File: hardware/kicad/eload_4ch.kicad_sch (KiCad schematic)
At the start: 0 parts

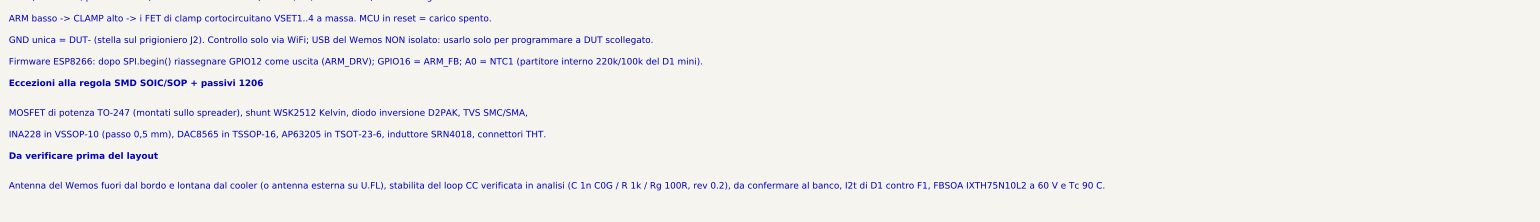
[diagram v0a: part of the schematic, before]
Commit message: rev 0.3: front panel with I2C OLED, encoder and OUTPUT button
PCF8574 expander (0x20) with INT on GPIO0, 10-pin IDC connector,
RC debounce, I2C pull-ups 2.2k, re-routed PCB (DRC/parity clean),
updated BOM, slides (front panel page) and README.

Co-Authored-By: Claude Opus 5.5 <noreply@anthropic.com>
Claude-Session: https://claude.ai/code/session_013KrwoEq2Y4F9LNKutY5RJ4
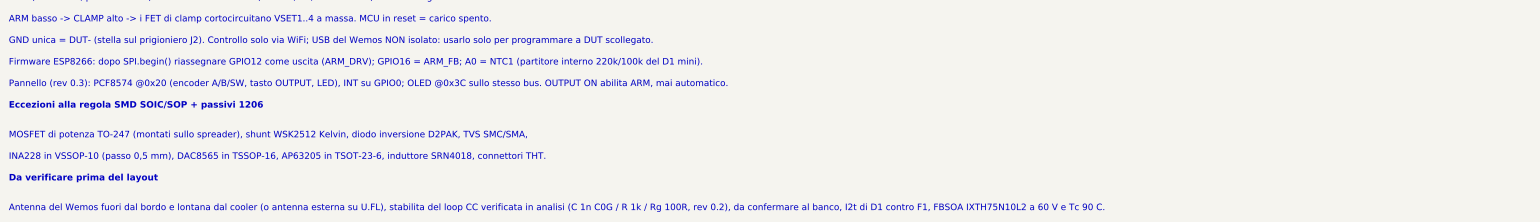
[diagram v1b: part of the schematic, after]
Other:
- note added: "Pannello (rev 0.3): PCF8574 @0x20 (encoder A/B/SW, tasto OUTPUT, LED), INT su GPIO0; OLED @0x3C sullo stesso bus. OUTPUT ON abilita ARM, mai automatico."
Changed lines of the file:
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@@
 		(title "Carico attivo 60V 20A 300W — Indice")
 		(date "2026-10-25")
-		(rev "0.2")
+		(rev "0.3")
 		(company "IV3HGA")
 		(comment 1 "Schema gerarchico: un foglio per blocco funzionale")
 	)
+	(text "GND unica = DUT- (stella sul prigioniero J2). Controllo solo via WiFi; USB del Wemos NON isolato: usarlo solo per programmare a DUT scollegato."
+		(exclude_from_sim no)
+		(at 30 212.32 0)
+		(effects
+			(font
+				(size 1.524 1.524)
+			)
+			(justify left bottom)
+		)
+	)
+	(text "Da verificare prima del layout"
+		(exclude_from_sim no)
+		(at 30 244.72 0)
+		(effects
+			(font
+				(size 1.524 1.524)
+				(bold yes)
+			)
+			(justify left bottom)
+		)
+	)
+	(text "Pannello (rev 0.3): PCF8574 @0x20 (encoder A/B/SW, tasto OUTPUT, LED), INT su GPIO0; OLED @0x3C sullo stesso bus. OUTPUT ON abilita ARM, mai automatico."
+		(exclude_from_sim no)
+		(at 30 222.48 0)
+		(effects
+			(font
+				(size 1.524 1.524)
+			)
+			(justify left bottom)
+		)
+	)
+	(text "MOSFET di potenza TO-247 (montati sullo spreader), shunt WSK2512 Kelvin, diodo inversione D2PAK, TVS SMC/SMA,"
+		(exclude_from_sim no)
+		(at 30 234.56 0)
+		(effects
+			(font
+				(size 1.524 1.524)
+			)
+			(justify left bottom)
+		)
+	)
+	(text "INA228 in VSSOP-10 (passo 0,5 mm), DAC8565 in TSSOP-16, AP63205 in TSOT-23-6, induttore SRN4018, connettori THT."
+		(exclude_from_sim no)
+		(at 30 239.64 0)
+		(effects
+			(font
+				(size 1.524 1.524)
+			)
+			(justify left bottom)
+		)
+	)
+	(text "Setpoint: DAC8565 0-2,5 V -> partitore 25:1 -> 0-100 mV su shunt 20 mOhm = 0-5 A. Il partitore e riferito al Kelvin freddo dello shunt (SHNx)."
+		(exclude_from_sim no)
+		(at 30 197.08 0)
+		(effects
+			(font
+				(size 1.524 1.524)
+			)
+			(justify left bottom)
+		)
+	)
+	(text "ARM basso -> CLAMP alto -> i FET di clamp cortocircuitano VSET1..4 a massa. MCU in reset = carico spento."
+		(exclude_from_sim no)
+		(at 30 207.24 0)
+		(effects
+			(font
+				(size 1.524 1.524)
+			)
+			(justify left bottom)
+		)
+	)
+	(text "Firmware ESP8266: dopo SPI.begin() riassegnare GPIO12 come uscita (ARM_DRV); GPIO16 = ARM_FB; A0 = NTC1 (partitore interno 220k/100k del D1 mini)."
+		(exclude_from_sim no)
+		(at 30 217.4 0)
+		(effects
+			(font
+				(size 1.524 1.524)
+			)
+			(justify left bottom)
+		)
+	)
 	(text "Carico elettronico 4 canali - 60 V / 20 A / 300 W"
 		(exclude_from_sim no)
@@
 		)
 	)
-	(text "Da verificare prima del layout"
-		(exclude_from_sim no)
-		(at 30 239.64 0)
+	(text "Antenna del Wemos fuori dal bordo e lontana dal cooler (o antenna esterna su U.FL), stabilita del loop CC verificata in analisi (C 1n C0G / R 1k / Rg 100R, rev 0.2), da confermare al banco, I2t di D1 contro F1, FBSOA IXTH75N10L2 a 60 V e Tc 90 C."
+		(exclude_from_sim no)
+		(at 30 251.72 0)
+		(effects
+			(font
+				(size 1.524 1.524)
+			)
+			(justify left bottom)
+		)
+	)
+	(text "Eccezioni alla regola SMD SOIC/SOP + passivi 1206"
+		(exclude_from_sim no)
+		(at 30 227.56 0)
 		(effects
 			(font
@@
 		)
 	)
-	(text "Setpoint: DAC8565 0-2,5 V -> partitore 25:1 -> 0-100 mV su shunt 20 mOhm = 0-5 A. Il partitore e riferito al Kelvin freddo dello shunt (SHNx)."
-		(exclude_from_sim no)
-		(at 30 197.08 0)
-		(effects
-			(font
-				(size 1.524 1.524)
-			)
-			(justify left bottom)
-		)
-	)
-	(text "INA228 in VSSOP-10 (passo 0,5 mm), DAC8565 in TSSOP-16, AP63205 in TSOT-23-6, induttore SRN4018, connettori THT."
-		(exclude_from_sim no)
-		(at 30 234.56 0)
-		(effects
-			(font
-				(size 1.524 1.524)
-			)
-			(justify left bottom)
-		)
-	)
-	(text "ARM basso -> CLAMP alto -> i FET di clamp cortocircuitano VSET1..4 a massa. MCU in reset = carico spento."
-		(exclude_from_sim no)
-		(at 30 207.24 0)
-		(effects
-			(font
-				(size 1.524 1.524)
-			)
-			(justify left bottom)
-		)
-	)
-	(text "Antenna del Wemos fuori dal bordo e lontana dal cooler (o antenna esterna su U.FL), stabilita del loop CC verificata in analisi (C 1n C0G / R 1k / Rg 100R, rev 0.2), da confermare al banco, I2t di D1 contro F1, FBSOA IXTH75N10L2 a 60 V e Tc 90 C."
-		(exclude_from_sim no)
-		(at 30 246.64 0)
-		(effects
-			(font
-				(size 1.524 1.524)
-			)
-			(justify left bottom)
-		)
-	)
 	(text "ARM (attivo alto, pull-down 10k) abilita il carico. LM393 (OVP 64,7 V, OTP ~100 C) e ALERT degli INA228 lo tirano basso in hardware."
 		(exclude_from_sim no)
@@
 		)
 	)
-	(text "MOSFET di potenza TO-247 (montati sullo spreader), shunt WSK2512 Kelvin, diodo inversione D2PAK, TVS SMC/SMA,"
-		(exclude_from_sim no)
-		(at 30 229.48 0)
-		(effects
-			(font
-				(size 1.524 1.524)
-			)
-			(justify left bottom)
-		)
-	)
-	(text "Firmware ESP8266: dopo SPI.begin() riassegnare GPIO12 come uscita (ARM_DRV); GPIO16 = ARM_FB; A0 = NTC1 (partitore interno 220k/100k del D1 mini)."
-		(exclude_from_sim no)
-		(at 30 217.4 0)
-		(effects
-			(font
-				(size 1.524 1.524)
-			)
-			(justify left bottom)
-		)
-	)
-	(text "GND unica = DUT- (stella sul prigioniero J2). Controllo solo via WiFi; USB del Wemos NON isolato: usarlo solo per programmare a DUT scollegato."
-		(exclude_from_sim no)
-		(at 30 212.32 0)
-		(effects
-			(font
-				(size 1.524 1.524)
-			)
-			(justify left bottom)
-		)
-	)
 	(text "Ogni canale: 0-5 A, max 75 W per MOSFET. Sopra 15 V il limite e la potenza (300 W / V), gestito da firmware + ALERT INA228."
 		(exclude_from_sim no)
@@
 		)
 	)
-	(text "Eccezioni alla regola SMD SOIC/SOP + passivi 1206"
-		(exclude_from_sim no)
-		(at 30 222.48 0)
-		(effects
-			(font
-				(size 1.524 1.524)
-				(bold yes)
-			)
-			(justify left bottom)
-		)
-	)
 	(sheet
-		(at 150 50)
+		(at 270 50)
 		(size 90 35)
 		(exclude_from_sim no)
@@
 			(color 0 0 0 0)
 		)
-		(property "Sheetname" "Canali di potenza"
-			(at 150 49.3 0)
+		(property "Sheetname" "Controllo"
+			(at 270 49.3 0)
 			(show_name no)
 			(do_not_autoplace no)
@@
 			)
 		)
-		(property "Sheetfile" "canali.kicad_sch"
-			(at 150 85.6 0)
+		(property "Sheetfile" "controllo.kicad_sch"
+			(at 270 85.6 0)
 			(show_name no)
 			(do_not_autoplace no)
@@
 		(instances
 			(project "eload_4ch"
-				(path "/080fc2a0-5c73-4662-b3f0-aee6c7395b8d"
-					(page "3")
+				(path "/28bb9797-67af-4466-82ad-11ee221e49cb"
+					(page "4")
 				)
 			)
@@
 	)
 	(sheet
-		(at 30 50)
+		(at 150 50)
 		(size 90 35)
 		(exclude_from_sim no)
@@
 			(color 0 0 0 0)
 		)
-		(property "Sheetname" "Ingresso e protezioni"
-			(at 30 49.3 0)
+		(property "Sheetname" "Canali di potenza"
+			(at 150 49.3 0)
 			(show_name no)
 			(do_not_autoplace no)
@@
 			)
 		)
-		(property "Sheetfile" "ingresso.kicad_sch"
-			(at 30 85.6 0)
+		(property "Sheetfile" "canali.kicad_sch"
+			(at 150 85.6 0)
 			(show_name no)
 			(do_not_autoplace no)
@@
 		(instances
 			(project "eload_4ch"
-				(path "/080fc2a0-5c73-4662-b3f0-aee6c7395b8d"
-					(page "2")
+				(path "/28bb9797-67af-4466-82ad-11ee221e49cb"
+					(page "3")
 				)
 			)
@@
 	)
 	(sheet
-		(at 270 50)
+		(at 30 110)
 		(size 90 35)
 		(exclude_from_sim no)
@@
 			(color 0 0 0 0)
 		)
-		(property "Sheetname" "Controllo"
-			(at 270 49.3 0)
+		(property "Sheetname" "Alimentazione"
+			(at 30 109.3 0)
 			(show_name no)
 			(do_not_autoplace no)
@@
 			)
 		)
-		(property "Sheetfile" "controllo.kicad_sch"
-			(at 270 85.6 0)
+		(property "Sheetfile" "alimentazione.kicad_sch"
+			(at 30 145.6 0)
 			(show_name no)
 			(do_not_autoplace no)
@@
 		(instances
 			(project "eload_4ch"
-				(path "/080fc2a0-5c73-4662-b3f0-aee6c7395b8d"
-					(page "4")
+				(path "/28bb9797-67af-4466-82ad-11ee221e49cb"
+					(page "5")
 				)
 			)
@@
 	)
 	(sheet
-		(at 30 110)
+		(at 30 50)
 		(size 90 35)
 		(exclude_from_sim no)
@@
 			(color 0 0 0 0)
 		)
-		(property "Sheetname" "Alimentazione"
-			(at 30 109.3 0)
+		(property "Sheetname" "Ingresso e protezioni"
+			(at 30 49.3 0)
 			(show_name no)
 			(do_not_autoplace no)
@@
 			)
 		)
-		(property "Sheetfile" "alimentazione.kicad_sch"
-			(at 30 145.6 0)
+		(property "Sheetfile" "ingresso.kicad_sch"
+			(at 30 85.6 0)
 			(show_name no)
 			(do_not_autoplace no)
@@
 		(instances
 			(project "eload_4ch"
-				(path "/080fc2a0-5c73-4662-b3f0-aee6c7395b8d"
-					(page "5")
-				)
-			)
+				(path "/28bb9797-67af-4466-82ad-11ee221e49cb"
+					(page "2")
+				)
+			)
